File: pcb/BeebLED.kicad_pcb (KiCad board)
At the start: 2 copper layers, 55.9 x 65.5 mm, 13 parts, among them J1 BBC User Port, J2 Jack-DC, J3 WS51282B, U1 74HC14, U2 74LS165, X1 8Mhz

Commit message: Fixed 8 Mhz not connected
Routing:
- net Net-(U2-Pad2): track 46.8 -> 50.1 mm
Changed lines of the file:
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@@
   (segment (start 100.34 72.38) (end 99.324 72.38) (width 0.25) (layer "B.Cu") (net 28))
   (segment (start 102.108 60.96) (end 102.108 70.612) (width 0.25) (layer "B.Cu") (net 28))
-  (segment (start 108.712 92.964) (end 101.6 92.964) (width 0.25) (layer "B.Cu") (net 29))
+  (segment (start 101.6 94.488) (end 101.6 77.196) (width 0.25) (layer "B.Cu") (net 29))
+  (segment (start 109.22 94.488) (end 101.6 94.488) (width 0.25) (layer "B.Cu") (net 29))
+  (segment (start 101.6 77.196) (end 99.324 74.92) (width 0.25) (layer "B.Cu") (net 29))
+  (segment (start 116.332 75.438) (end 116.332 77.724) (width 0.25) (layer "B.Cu") (net 29))
   (segment (start 116.332 77.724) (end 109.22 84.836) (width 0.25) (layer "B.Cu") (net 29))
-  (segment (start 101.6 92.964) (end 101.6 77.196) (width 0.25) (layer "B.Cu") (net 29))
-  (segment (start 116.332 75.438) (end 116.332 77.724) (width 0.25) (layer "B.Cu") (net 29))
-  (segment (start 109.22 84.836) (end 109.22 92.456) (width 0.25) (layer "B.Cu") (net 29))
-  (segment (start 101.6 77.196) (end 99.324 74.92) (width 0.25) (layer "B.Cu") (net 29))
-  (segment (start 109.22 92.456) (end 108.712 92.964) (width 0.25) (layer "B.Cu") (net 29))
+  (segment (start 109.22 84.836) (end 109.22 94.488) (width 0.25) (layer "B.Cu") (net 29))
   (segment (start 112.776 56.622) (end 112.776 60.452) (width 0.25) (layer "F.Cu") (net 34))
   (segment (start 112.776 56.622) (end 106.954 56.622) (width 0.25) (layer "F.Cu") (net 34))

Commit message: Changed J3 connector type and tied U1 Pin 3 to GND
Thanks to the advice from stardot! :-)
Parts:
- J3: footprint Connector_JST:JST_EH_S3B-EH_1x03_P2.50mm_Horizontal -> Connector_JST:JST_PH_S3B-PH-K_1x03_P2.00mm_Horizontal
- moved J3 5.01 mm to (129.0, 94.5), turned to 90 degrees
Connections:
- U1 pad 3: unconnected-(U1-Pad3) -> GND
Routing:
- net +5V: track 124.5 -> 121.4 mm

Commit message: Added support for DIP8 crystal
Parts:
- added X2: Oscillator_DIP-8, Oscillator:Oscillator_DIP-8, F.Cu at (127.8, 67.8)
- moved J3 0.60 mm to (129.6, 94.5)
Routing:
- net Net-(U2-Pad2): track 50.1 -> 53.9 mm
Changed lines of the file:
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@@
       (effects (font (size 1 1) (thickness 0.15)))
     )
-    (fp_text value "Jack-DC" (at 0 13 90) (layer "F.Fab")
+    (fp_text value "Jack-DC" (at -8.128 7.032) (layer "F.SilkS")
       (effects (font (size 1 1) (thickness 0.15)))
     )
@@
       (effects (font (size 1 1) (thickness 0.15)))
     )
-    (fp_text user "K" (at 0 -1.9 180) (layer "F.SilkS")
-      (effects (font (size 1 1) (thickness 0.15)))
-    )
-    (fp_text user "K" (at 0 -1.9 180) (layer "F.Fab")
+    (fp_text user "K" (at 0 2.032 180) (layer "F.SilkS")
+      (effects (font (size 1 1) (thickness 0.15)))
+    )
+    (fp_text user "K" (at 0 2.032 180) (layer "F.Fab")
       (effects (font (size 1 1) (thickness 0.15)))
     )
@@
     )
   )
+  (footprint "Oscillator:Oscillator_DIP-8" (layer "F.Cu")
+    (at 127.789725 67.849704 180)
+    (descr "Oscillator, DIP8,http://cdn-reichelt.de/documents/datenblatt/B400/OSZI.pdf")
+    (tags "oscillator")
+    (attr through_hole)
+    (fp_text reference "X2" (at 3.81 -11.26) (layer "F.SilkS") hide
+      (effects (font (size 1 1) (thickness 0.15)))
+    )
+    (fp_text value "Oscillator_DIP-8" (at 3.81 3.74) (layer "F.Fab") hide
+      (effects (font (size 1 1) (thickness 0.15)))
+    )
+    (fp_text user "${REFERENCE}" (at 3.81 -3.81) (layer "F.Fab") hide
+      (effects (font (size 1 1) (thickness 0.15)))
+    )
+    (fp_line (start -1.54 1.54) (end -1.54 -8.81) (layer "F.SilkS") (width 0.1))
+    (fp_line (start -1.54 1.54) (end 8.81 1.54) (layer "F.SilkS") (width 0.1))
+    (fp_line (start 9.16 1.19) (end 9.16 -8.81) (layer "F.SilkS") (width 0.1))
+    (fp_line (start -1.19 -9.16) (end 8.81 -9.16) (layer "F.SilkS") (width 0.1))
+    (fp_arc (start -1.54 -8.81) (mid -1.437487 -9.057487) (end -1.19 -9.16) (layer "F.SilkS") (width 0.1))
+    (fp_arc (start 8.81 -9.16) (mid 9.057487 -9.057487) (end 9.16 -8.81) (layer "F.SilkS") (width 0.1))
+    (fp_arc (start 9.16 1.19) (mid 9.057487 1.437487) (end 8.81 1.54) (layer "F.SilkS") (width 0.1))
+    (fp_line (start -2.79 -10.41) (end -2.79 2.79) (layer "F.CrtYd") (width 0.05))
+    (fp_line (start -2.79 2.79) (end 10.41 2.79) (layer "F.CrtYd") (width 0.05))
+    (fp_line (start 10.41 -10.41) (end -2.79 -10.41) (layer "F.CrtYd") (width 0.05))
+    (fp_line (start 10.41 2.79) (end 10.41 -10.41) (layer "F.CrtYd") (width 0.05))
+    (fp_line (start -1.89 -10.16) (end 9.51 -10.16) (layer "F.Fab") (width 0.1))
+    (fp_line (start -2.54 2.54) (end -2.54 -9.51) (layer "F.Fab") (width 0.1))
+    (fp_line (start 10.16 -9.51) (end 10.16 1.89) (layer "F.Fab") (width 0.1))
+    (fp_line (start -2.54 2.54) (end 9.51 2.54) (layer "F.Fab") (width 0.1))
+    (fp_arc (start 9.51 -10.16) (mid 9.969619 -9.969619) (end 10.16 -9.51) (layer "F.Fab") (width 0.1))
+    (fp_arc (start 10.16 1.89) (mid 9.969619 2.349619) (end 9.51 2.54) (layer "F.Fab") (width 0.1))
+    (fp_arc (start -2.54 -9.51) (mid -2.349619 -9.969619) (end -1.89 -10.16) (layer "F.Fab") (width 0.1))
+    (pad "1" thru_hole rect (at 0 0 180) (size 1.6 1.6) (drill 0.8) (layers *.Cu *.Mask))
+    (pad "4" thru_hole circle (at 7.62 0 180) (size 1.6 1.6) (drill 0.8) (layers *.Cu *.Mask)
+      (net 2 "GND"))
+    (pad "5" thru_hole circle (at 7.62 -7.62 180) (size 1.6 1.6) (drill 0.8) (layers *.Cu *.Mask)
+      (net 29 "Net-(U2-Pad2)"))
+    (pad "8" thru_hole circle (at 0 -7.62 180) (size 1.6 1.6) (drill 0.8) (layers *.Cu *.Mask)
+      (net 3 "+5V"))
+    (model "${KICAD6_3DMODEL_DIR}/Oscillator.3dshapes/Oscillator_DIP-8.wrl"
+      (offset (xyz 0 0 0))
+      (scale (xyz 1 1 1))
+      (rotate (xyz 0 0 0))
+    )
+  )
   (footprint "Connector_JST:JST_PH_S3B-PH-K_1x03_P2.00mm_Horizontal" (layer "F.Cu")
-    (at 129.032 94.456 90)
+    (at 129.63 94.456 90)
     (descr "JST PH series connector, S3B-PH-K (http://www.jst-mfg.com/product/pdf/eng/ePH.pdf), generated with kicad-footprint-generator")
     (tags "connector JST PH top entry")
@@
   (segment (start 89.408 56.388) (end 89.408 79.248) (width 0.25) (layer "F.Cu") (net 7))
   (segment (start 96.032 55.88) (end 94.996 55.88) (width 0.25) (layer "F.Cu") (net 7))
-  (segment (start 128.524 92.456) (end 129.032 91.948) (width 0.25) (layer "F.Cu") (net 23))
-  (segment (start 122.936 92.456) (end 128.524 92.456) (width 0.25) (layer "F.Cu") (net 23))
+  (segment (start 122.936 92.456) (end 129.63 92.456) (width 0.25) (layer "F.Cu") (net 23))
   (segment (start 110.48 90.16) (end 112.776 92.456) (width 0.25) (layer "F.Cu") (net 24))
   (segment (start 106.944 90.16) (end 110.48 90.16) (width 0.25) (layer "F.Cu") (net 24))
@@
   (segment (start 109.22 94.488) (end 101.6 94.488) (width 0.25) (layer "B.Cu") (net 29))
   (segment (start 101.6 77.196) (end 99.324 74.92) (width 0.25) (layer "B.Cu") (net 29))
+  (segment (start 120.142 75.438) (end 116.332 75.438) (width 0.25) (layer "B.Cu") (net 29))
   (segment (start 116.332 75.438) (end 116.332 77.724) (width 0.25) (layer "B.Cu") (net 29))
   (segment (start 116.332 77.724) (end 109.22 84.836) (width 0.25) (layer "B.Cu") (net 29))

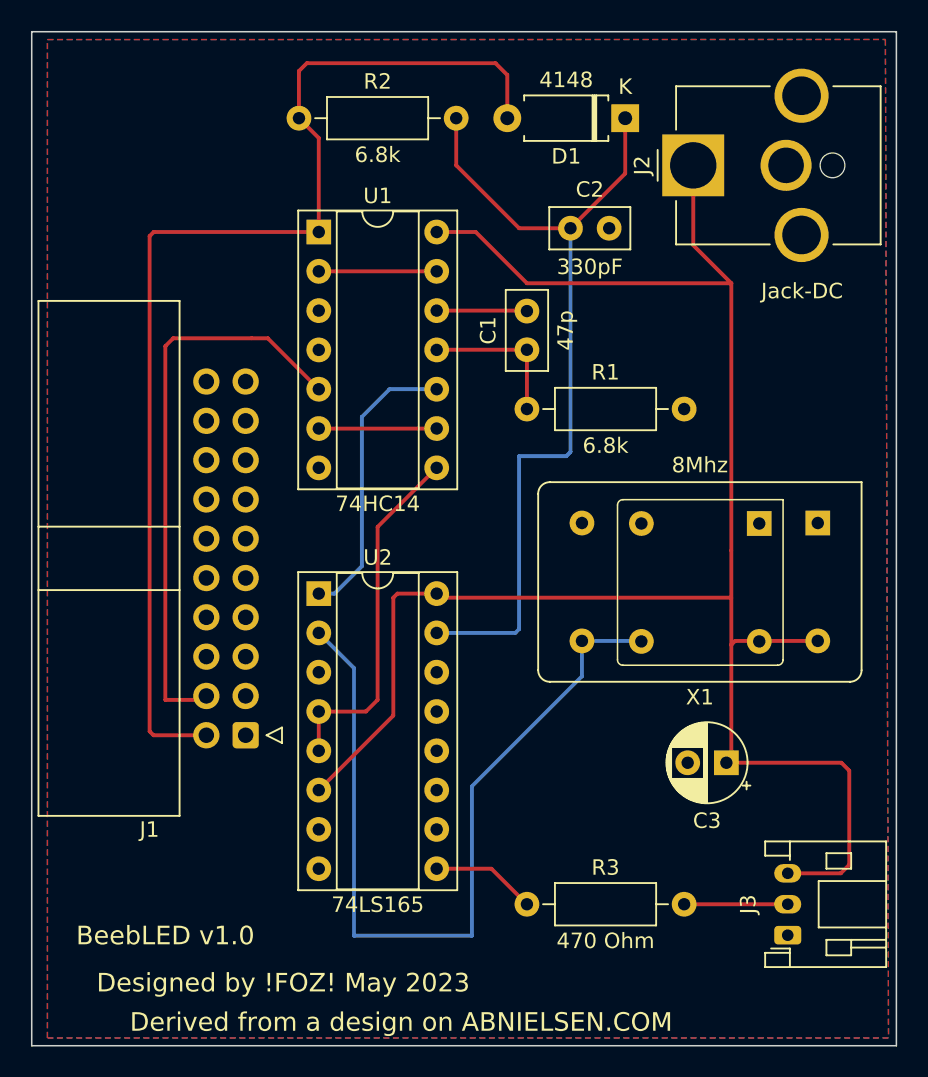
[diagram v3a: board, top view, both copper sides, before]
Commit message: Added alternative X2 component to schema and updated PCB
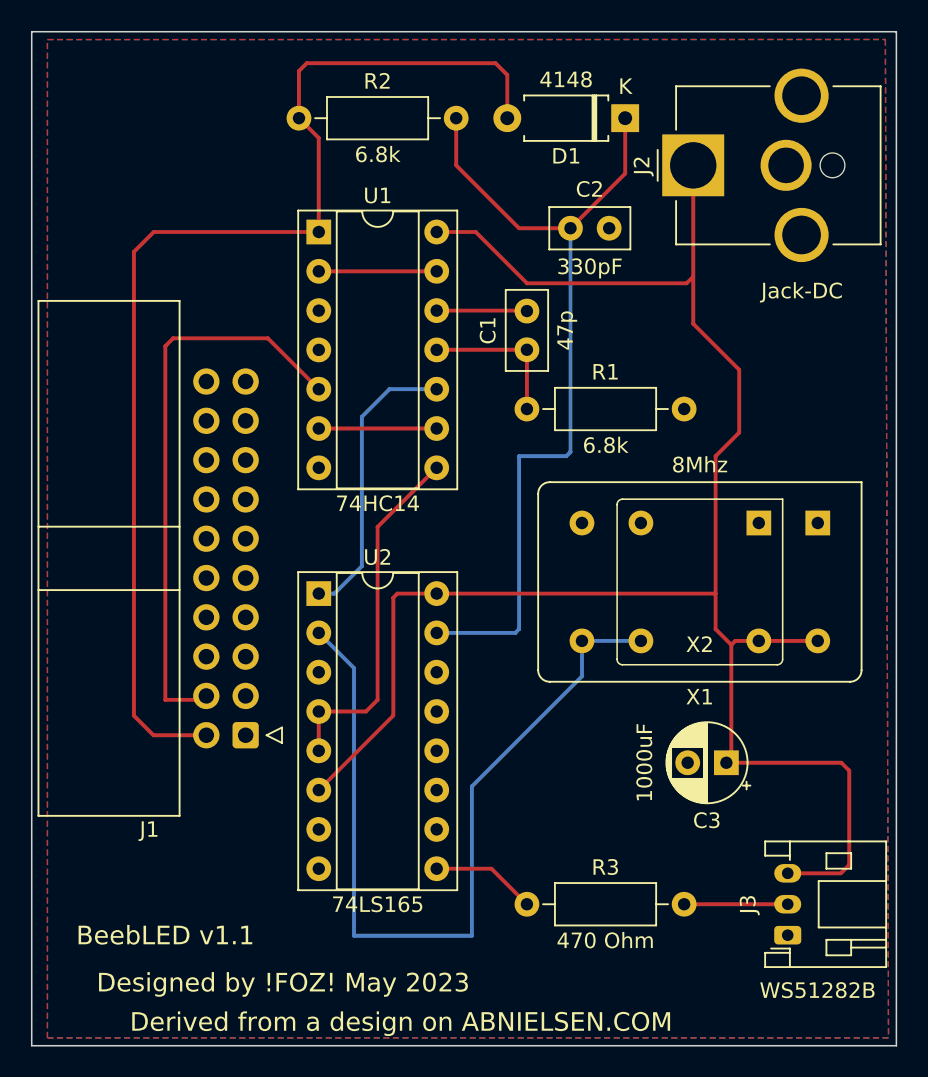
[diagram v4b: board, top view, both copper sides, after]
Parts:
- X2: value Oscillator_DIP-8 -> 8Mhz
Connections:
- X2 pad 1: (no net) -> unconnected-(X2-Pad1)
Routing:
- net +5V: track 121.4 -> 119.3 mm
- net Net-(D1-Pad2): track 74.5 -> 75.4 mm
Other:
- board text added: "BeebLED v1.1"
- board text removed: "BeebLED v1.0"
